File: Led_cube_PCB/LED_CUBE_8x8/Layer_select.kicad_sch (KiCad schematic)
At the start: 2 parts, among them IC31 74AHC138PW,118

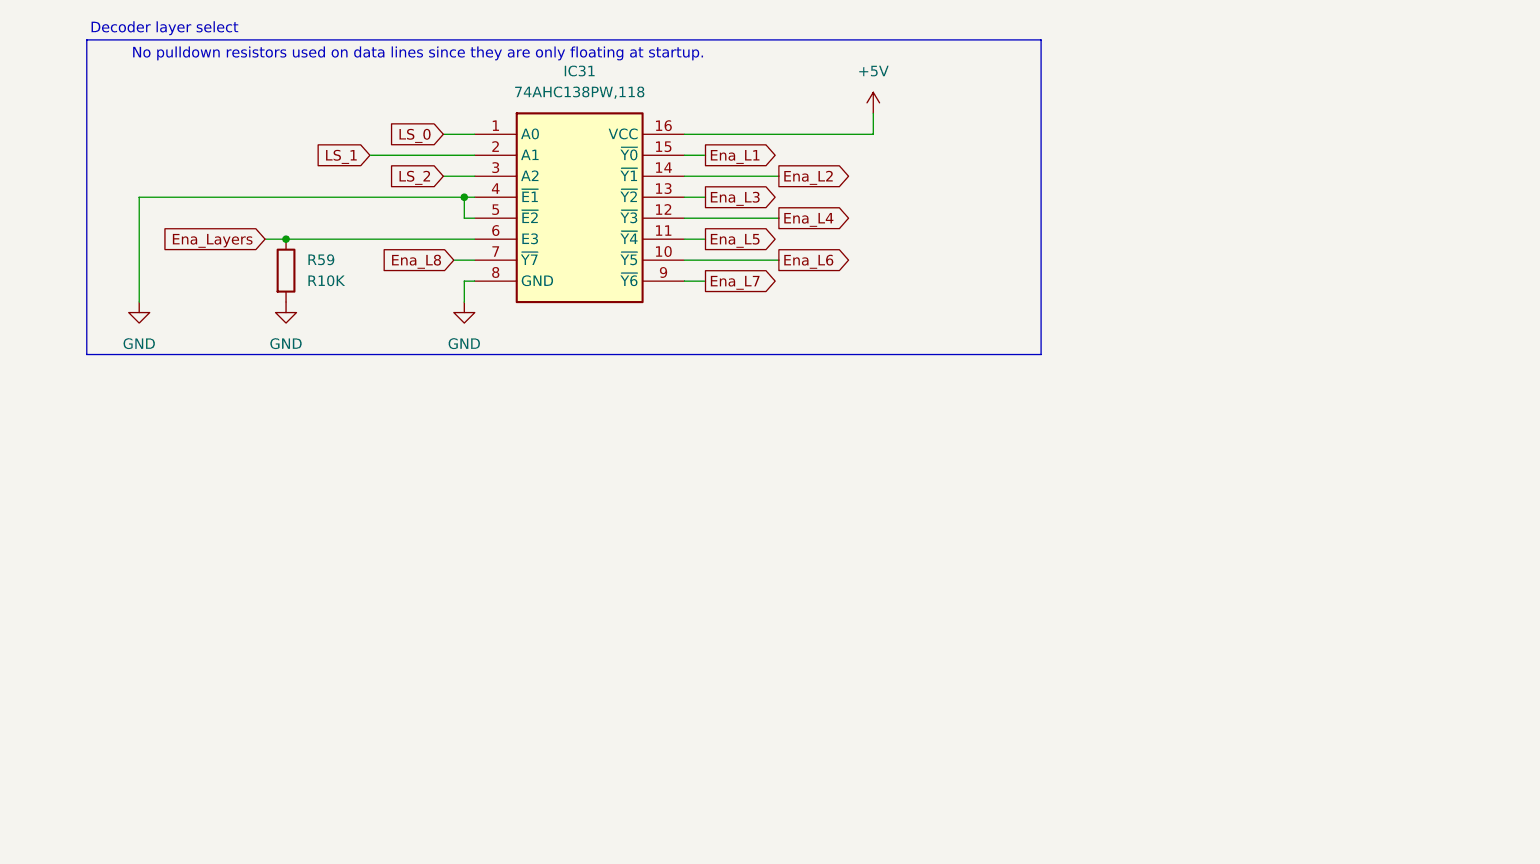
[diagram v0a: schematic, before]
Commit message: added spice simulations folder, For simulating transients effect on the power buck converter. Also finished layer select in eeschema.
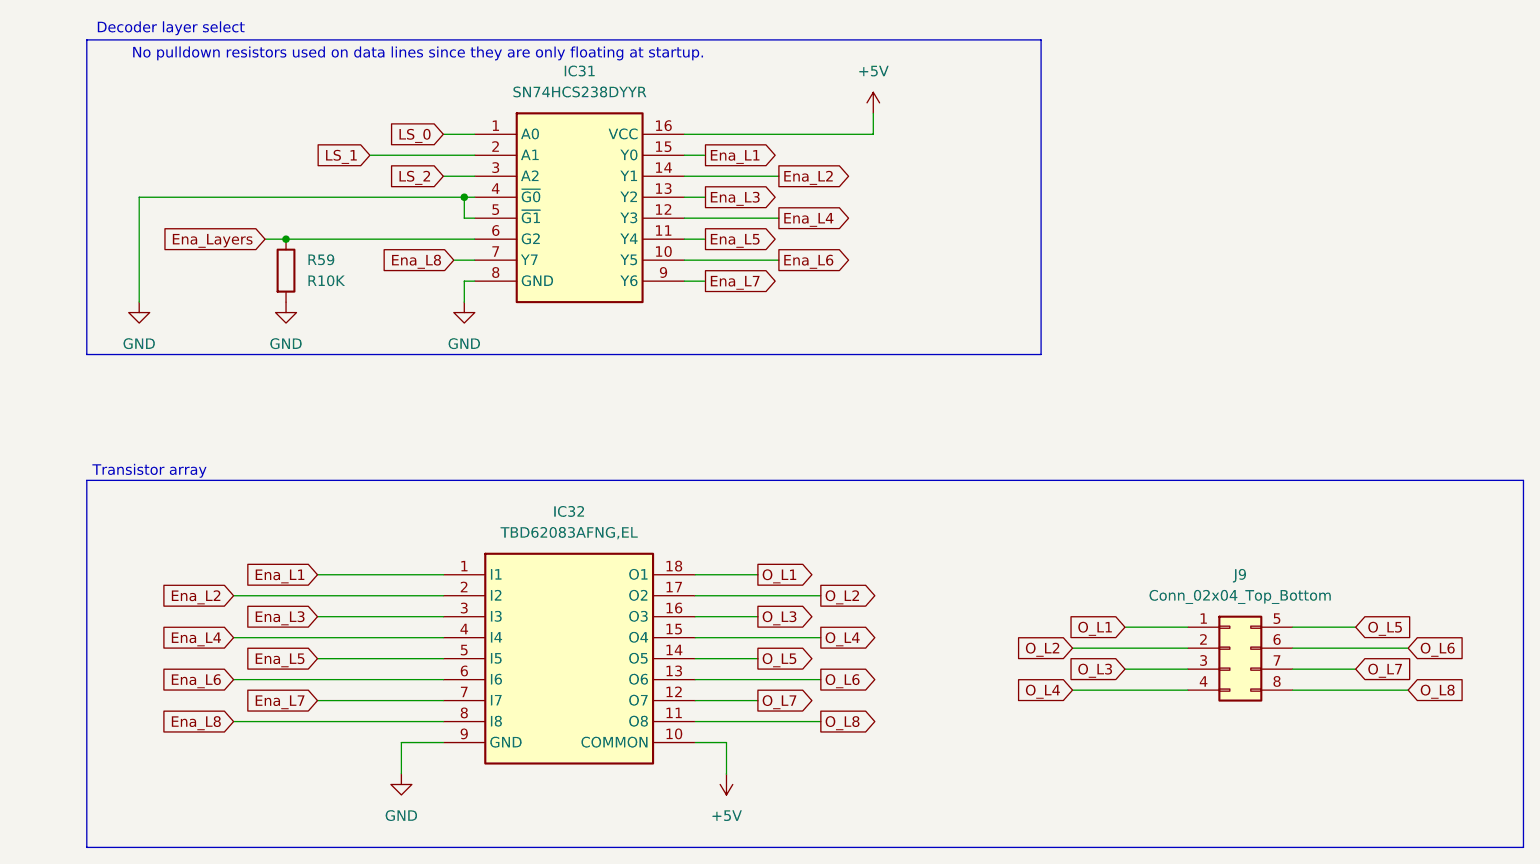
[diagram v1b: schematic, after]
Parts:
- removed IC31: 74AHC138PW,118, SOP65P640X110-16N, symbol SamacSys_Parts:74AHC138PW,118
- added IC31: SN74HCS238DYYR, SOP50P326X110-16N, symbol SamacSys_Parts:SN74HCS238DYYR
- added IC32: TBD62083AFNG,EL, SOIC127P1030X245-18N, symbol SamacSys_Parts:TBD62083AFNG,EL
- added J9: Conn_02x04_Top_Bottom, Connector_PinHeader_2.54mm:PinHeader_2x04_P2.54mm_Vertical, symbol Connector_Generic:Conn_02x04_Top_Bottom
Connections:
- net +5V: now also IC31.16 (VCC), IC32.10 (COMMON)
- net Ena_L1: now also IC31.15 (Y0), IC32.1 (I1)
- net Ena_L2: now also IC31.14 (Y1), IC32.2 (I2)
- net Ena_L3: now also IC31.13 (Y2), IC32.3 (I3)
- net Ena_L4: now also IC31.12 (Y3), IC32.4 (I4)
- net Ena_L5: now also IC31.11 (Y4), IC32.5 (I5)
- net Ena_L6: now also IC31.10 (Y5), IC32.6 (I6)
- net Ena_L7: now also IC31.9 (Y6), IC32.7 (I7)
- net Ena_L8: now also IC31.7 (Y7), IC32.8 (I8)
- net Ena_Layers: now also IC31.6 (G2)
- net GND: now also IC31.4 (~{G0}), IC31.5 (~{G1}), IC31.8 (GND), IC32.9 (GND)
- net LS_0: now also IC31.1 (A0)
- net LS_1: now also IC31.2 (A1)
- net LS_2: now also IC31.3 (A2)
- new net O_L1: IC32.18 (O1), J9.1 (Pin_1)
- new net O_L2: IC32.17 (O2), J9.2 (Pin_2)
- new net O_L3: IC32.16 (O3), J9.3 (Pin_3)
- new net O_L4: IC32.15 (O4), J9.4 (Pin_4)
- new net O_L5: IC32.14 (O5), J9.5 (Pin_5)
- new net O_L6: IC32.13 (O6), J9.6 (Pin_6)
- new net O_L7: IC32.12 (O7), J9.7 (Pin_7)
- new net O_L8: IC32.11 (O8), J9.8 (Pin_8)
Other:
- note added: "Transistor array"
